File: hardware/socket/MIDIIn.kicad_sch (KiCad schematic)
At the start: 4 parts, among them J201 NE8FAH, U201 THVD2442

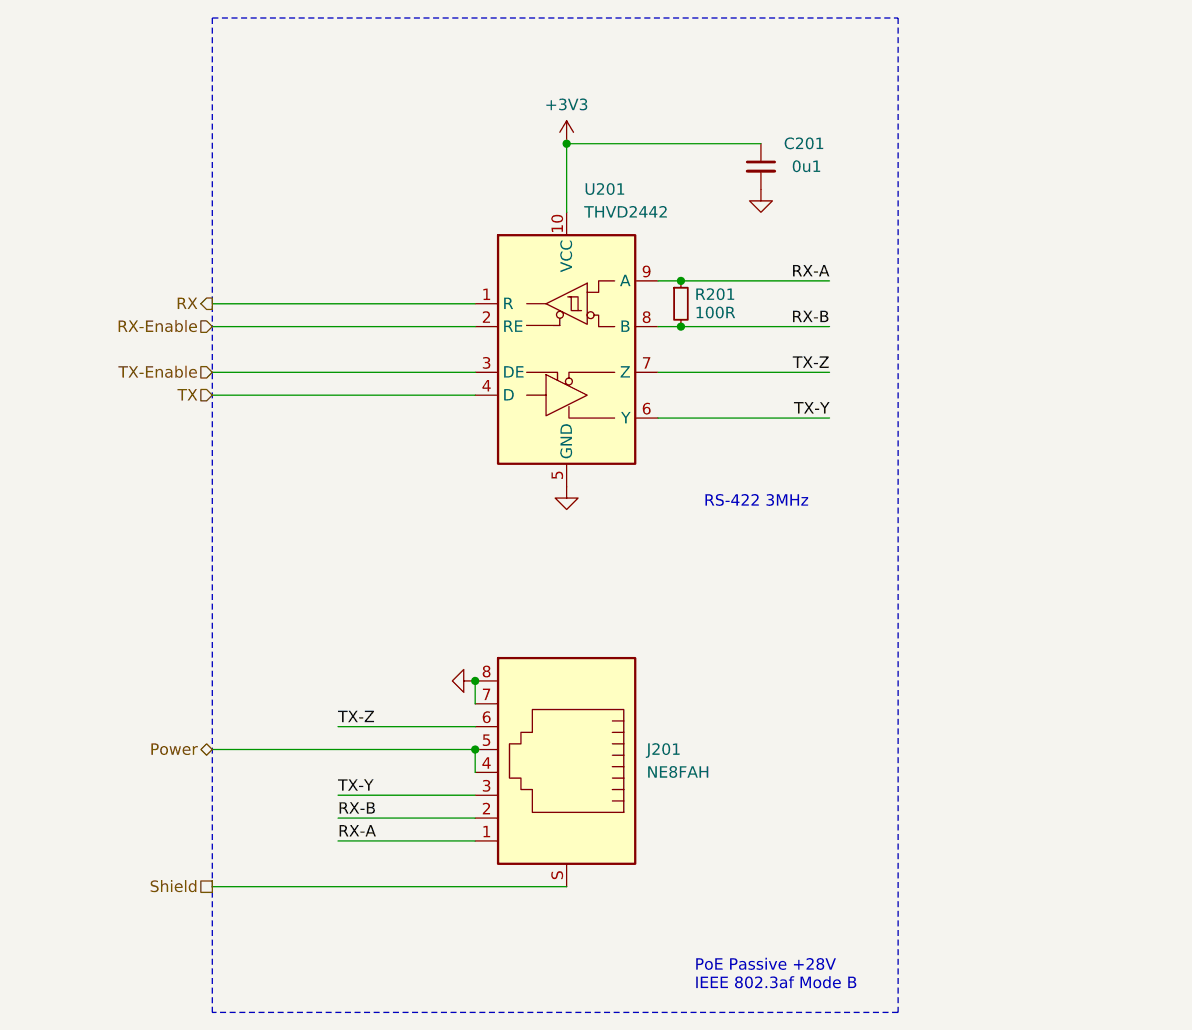
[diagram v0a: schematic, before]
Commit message: Split into socket and plug
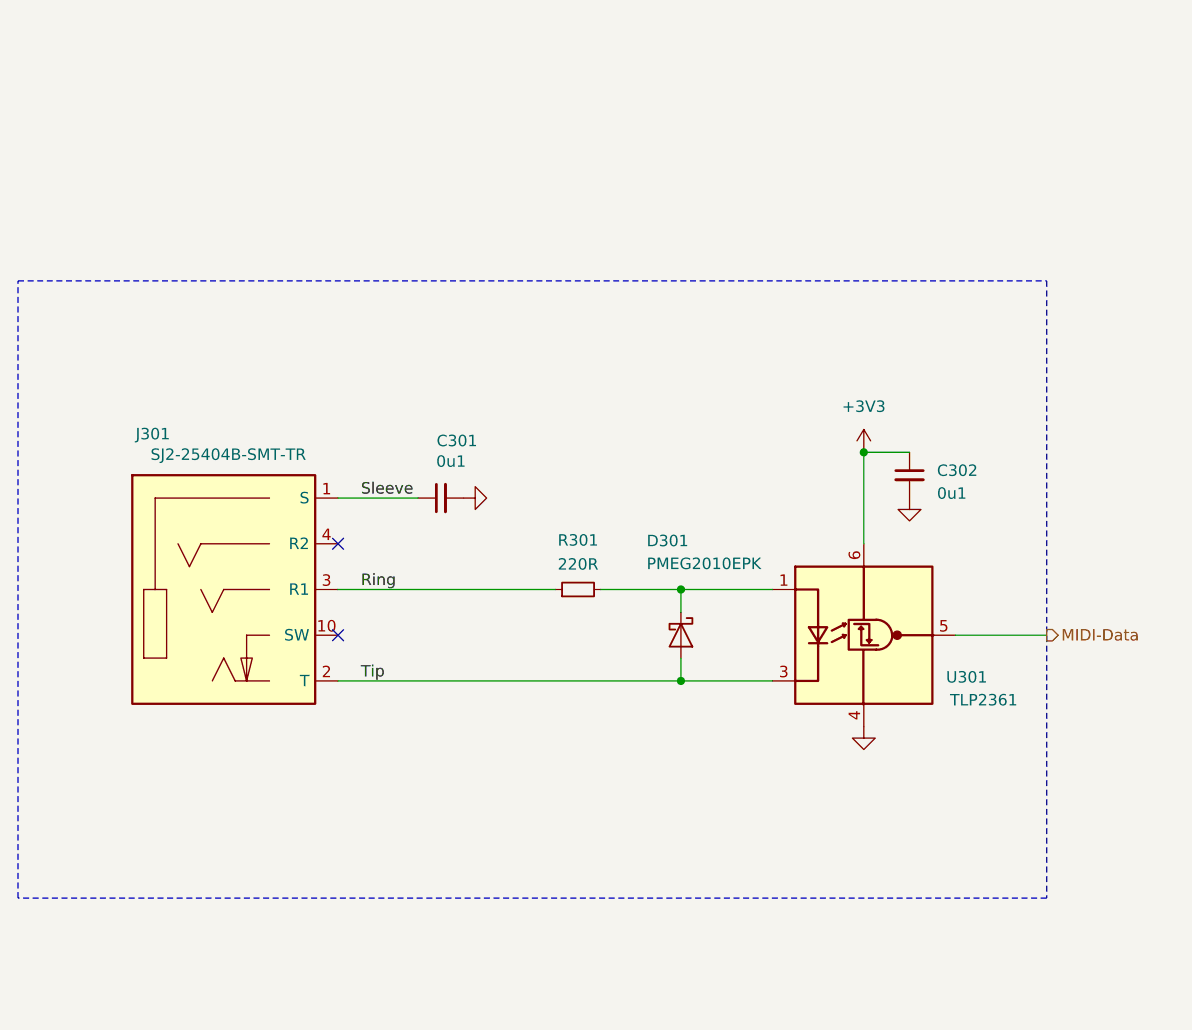
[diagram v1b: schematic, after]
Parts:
- removed C201: 0u1, V2_Capacitor_SMD:C_0603, symbol V2_Capacitor:0603_0u1
- removed J201: NE8FAH, V2_Connector_EtherCon:NE8FAH, symbol V2_Connector_EtherCon:NE8FAH
- removed R201: 100R, V2_Resistor_SMD:R_0603, symbol V2_Resistor:0603_100R
- removed U201: THVD2442, V2_Package_SON:VSON-10-4-1EP_3x3mm_P0.5mm_EP1.65x2.4mm_ThermalVias, symbol V2_Interface_RS485:THVD2442
- added C301, C302: 0u1, V2_Capacitor_SMD:C_0603, symbol V2_Capacitor:0603_0u1
- added D301: PMEG2010EPK, V2_Diode_SMD:D_SOD-1608, symbol V2_Diode:PMEG2010EPK
- added J301: SJ2-25404B-SMT-TR, V2_Connector_Audio:CUI_SJ2-25404B-SMT-TR, symbol V2_Connector_Audio:SJ2-25404B-SMT-TR
- added R301: 220R, V2_Resistor_SMD:R_0603, symbol V2_Resistor:0603_220R
- added U301: TLP2361, V2_Package_SO:SO-5-6_4.55x3.7mm_P1.27mm, symbol V2_Isolator:TLP2361
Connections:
- net +3V3: now also C302.1, U301.6 (VDD)
- net GND: now also C301.2, C302.2, U301.4 (GND)
- new net: D301.1 (K), R301.2, U301.1 (A)
- new net MIDI-Data: U301.5 (VO)
- new net Ring: J301.3 (R1), R301.1
- new net Sleeve: C301.1, J301.1 (S)
- new net Tip: D301.2 (A), J301.2 (T), U301.3 (K)
- no-connect marks 0 -> 2
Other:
- note removed: "PoE Passive +28V IEEE 802.3af Mode B"
- note removed: "RS-422 3MHz"
- title: V2 connect -> V2 connect-socket

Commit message: Good Bye Imperial
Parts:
- C301, C302: footprint V2_Capacitor_SMD:C_0603 -> V2_Capacitor_SMD:C_1608; symbol V2_Capacitor:0603_0u1 -> V2_Capacitor:1608_0u1
- R301: footprint V2_Resistor_SMD:R_0603 -> V2_Resistor_SMD:R_1608; symbol V2_Resistor:0603_220R -> V2_Resistor:1608_220R
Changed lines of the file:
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@@
 	(title_block
 		(title "V2 connect-socket")
-		(date "2026-04-23")
+		(date "2026-05-11")
 		(rev "2026-04-23")
 		(company "Versio Duo")
